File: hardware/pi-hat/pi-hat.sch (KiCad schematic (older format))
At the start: 100 parts, among them J1 PWR_IN, J10 6-8, J11 LED0, J12 LED1, J13 KLPX-0848A-2-B, J14 KLPX-0848A-2-R, J2 A-F, J3 40HAT, J4 G-M, J5 N-Q, J6 PANEL_PWR, J7 PANEL_CTL, J8 2-5, J9 WP, Q1 DMG2305UX, Q2 DMMT5401, Q3 DMN6075S, Q4 DMP4065S, Q5 DMN6075S, U1 CAT24C32, U10 L78L33_SOT89, U11 L78L33_SOT89, U12 PCM5122PW, U13 TSR_2-2450, U14 TSR_2-2450, U15 TSR_2-2450, U2 CM1293A, U3 CM1293A, U4 CM1293A, U5 CM1293A, U6 CM1293A, U7 CM1293A, U8 MCP23S17_SO, U9 MCP23S17_SO

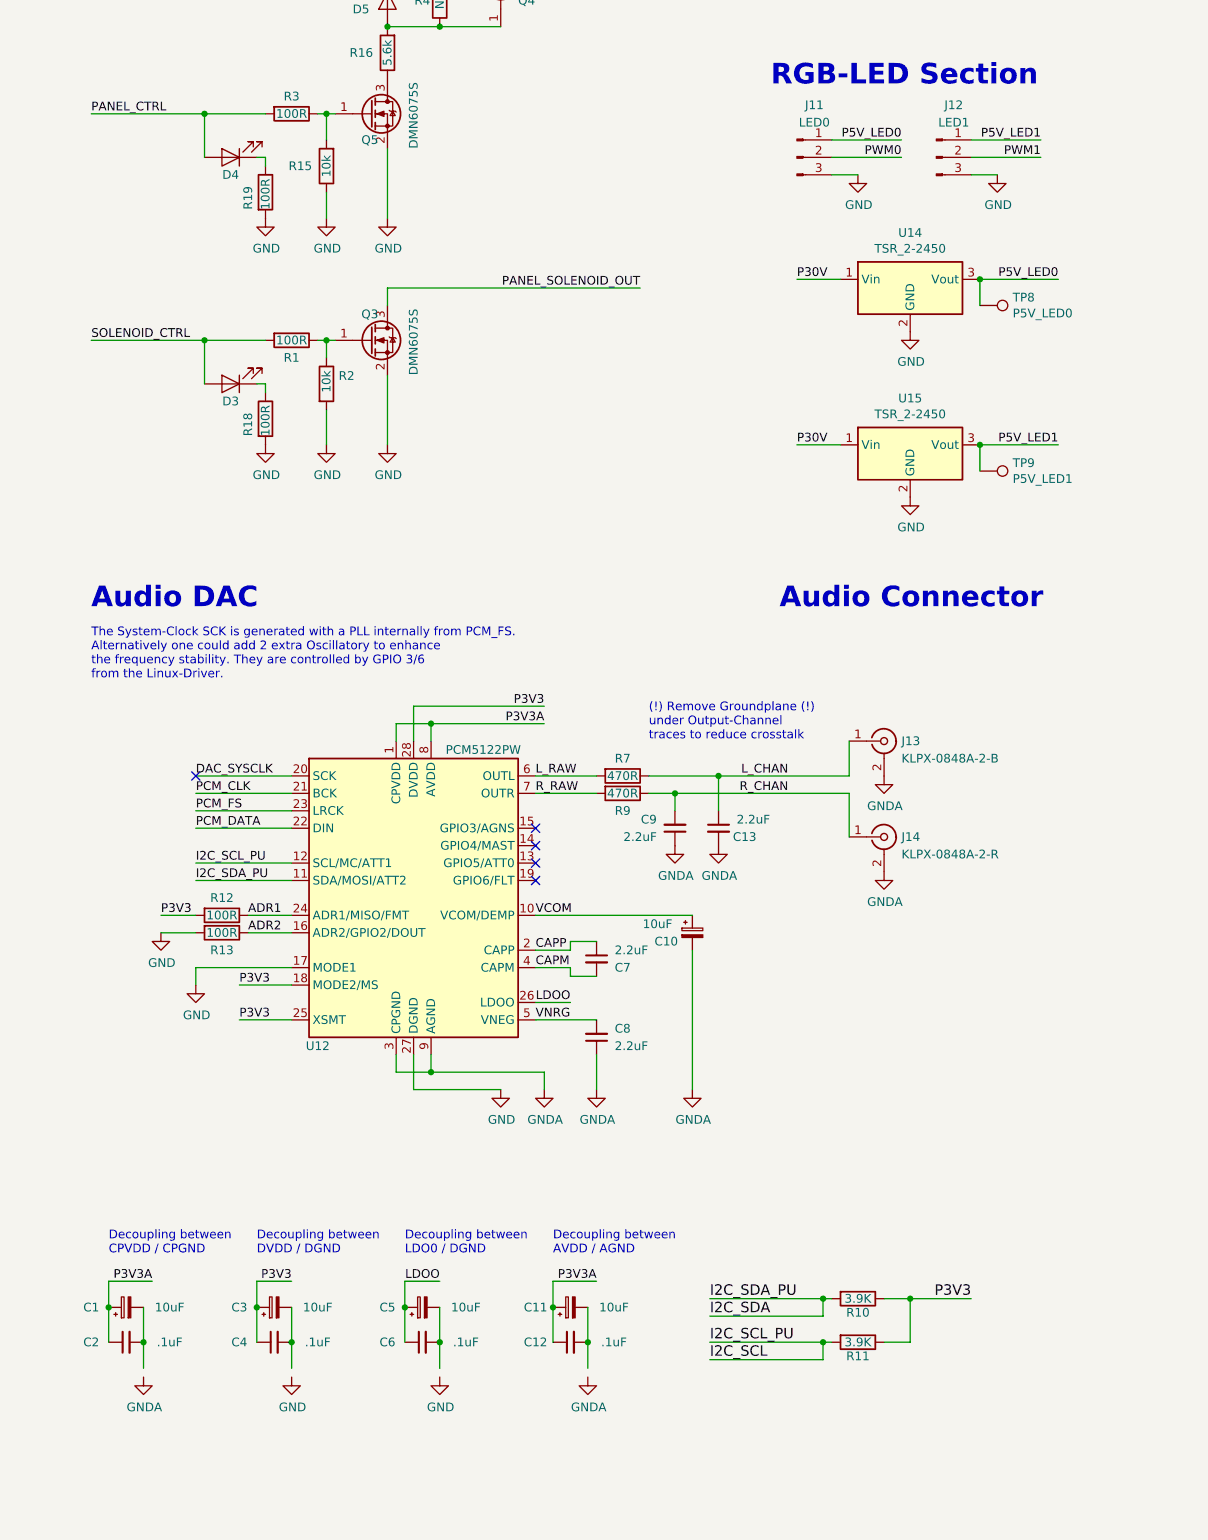
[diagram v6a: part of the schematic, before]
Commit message: fix broken gnd, only install a single 5V 2A DC/DC for the LEDs
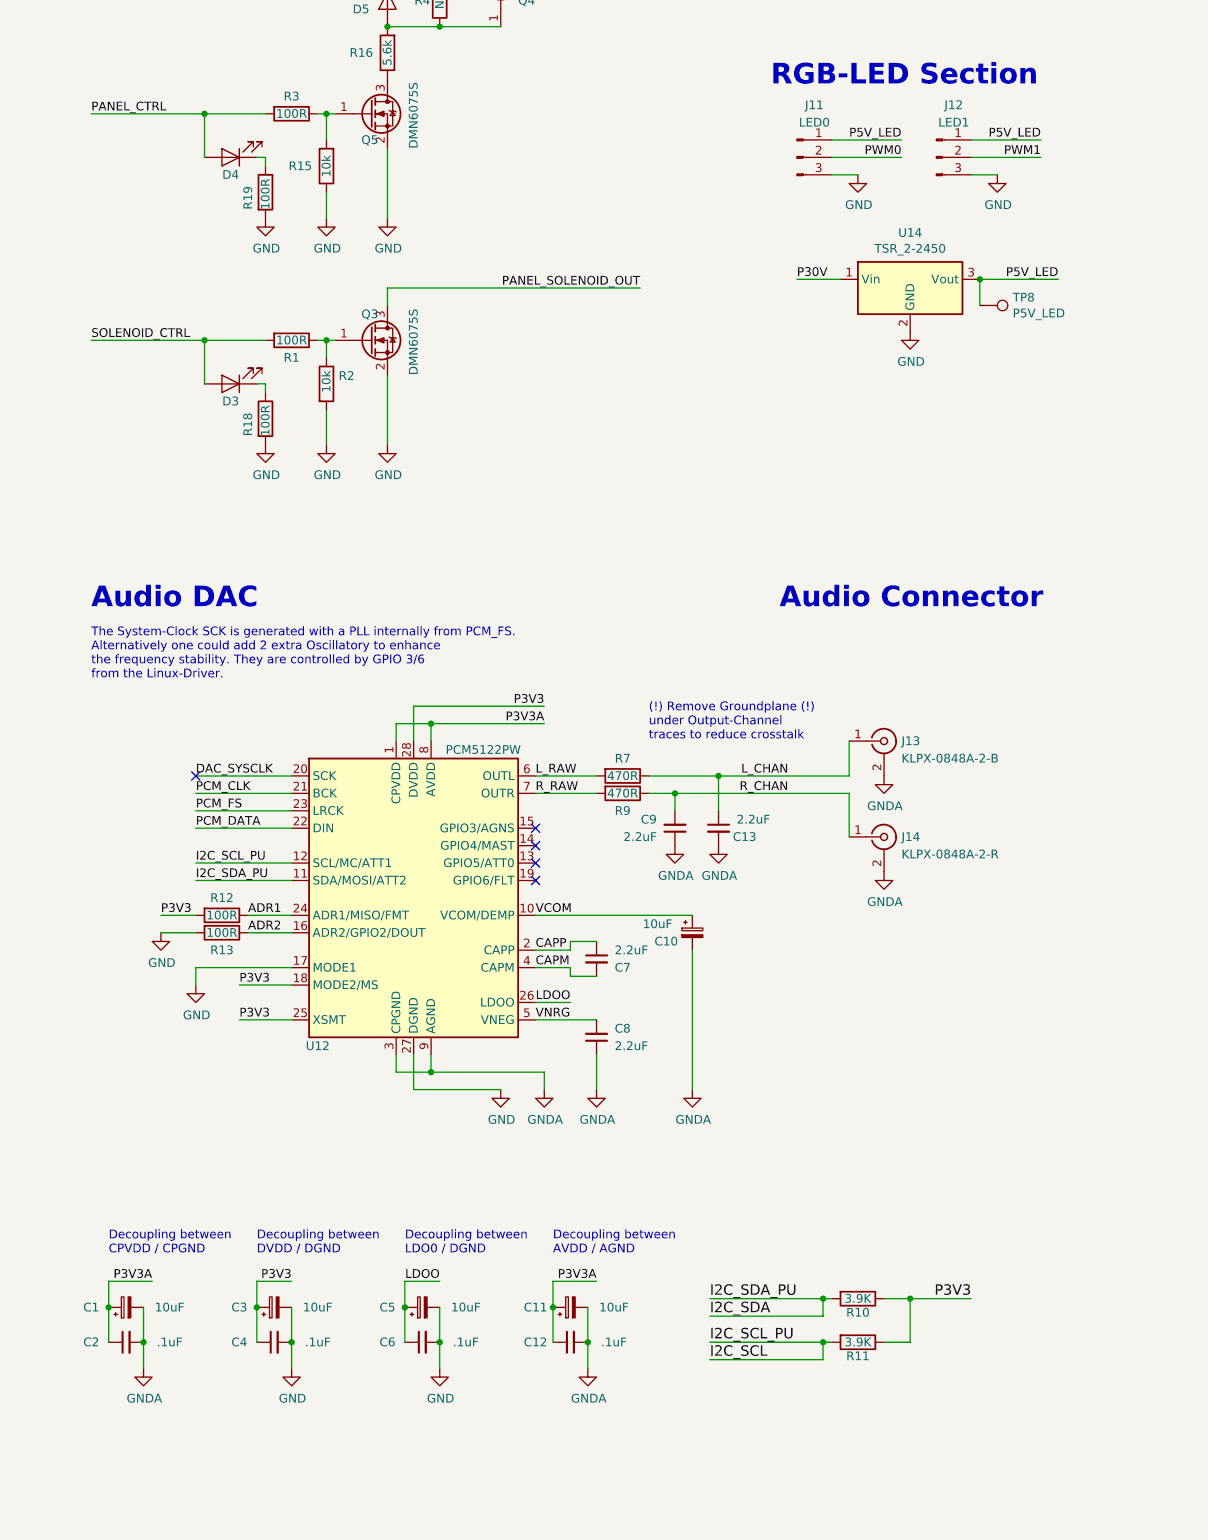
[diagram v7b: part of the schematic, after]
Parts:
- removed TP9: P5V_LED1, TestPoint:TestPoint_Pad_D1.5mm, symbol Connector:TestPoint
- removed U15: TSR_2-2450, Converter_DCDC:Converter_DCDC_TRACO_TSR-1_THT, symbol Regulator_Switching:TSR_1-2450
- TP8: value P5V_LED0 -> P5V_LED
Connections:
- net P5V_LED1 is gone; now on net P5V_LED: J12.1 (Pin_1)
- net GND: now also C3.2, C4.2, C5.2, C6.2
- net GNDA: now also C1.2, C11.2, C12.2, C2.2
- net P5V_LED0 renamed P5V_LED
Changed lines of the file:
@@
 L power:GND #PWR0109
 U 1 1 60FE9052
-P 6300 13200
-F 0 "#PWR0109" H 6300 12950 50  0001 C CNN
-F 1 "GND" H 6305 13027 50  0000 C CNN
-F 2 "" H 6300 13200 50  0001 C CNN
-F 3 "" H 6300 13200 50  0001 C CNN
-	1    6300 13200
+P 6300 13150
+F 0 "#PWR0109" H 6300 12900 50  0001 C CNN
+F 1 "GND" H 6305 12977 50  0000 C CNN
+F 2 "" H 6300 13150 50  0001 C CNN
+F 3 "" H 6300 13150 50  0001 C CNN
+	1    6300 13150
 	1    0    0    -1
 $EndComp
@@
 L power:GND #PWR0110
 U 1 1 610983C0
-P 7150 13200
-F 0 "#PWR0110" H 7150 12950 50  0001 C CNN
-F 1 "GND" H 7155 13027 50  0000 C CNN
-F 2 "" H 7150 13200 50  0001 C CNN
-F 3 "" H 7150 13200 50  0001 C CNN
-	1    7150 13200
+P 7150 13150
+F 0 "#PWR0110" H 7150 12900 50  0001 C CNN
+F 1 "GND" H 7155 12977 50  0000 C CNN
+F 2 "" H 7150 13150 50  0001 C CNN
+F 3 "" H 7150 13150 50  0001 C CNN
+	1    7150 13150
 	1    0    0    -1
 $EndComp
@@
 L power:GNDA #PWR0111
 U 1 1 6124BBFC
-P 5450 13200
-F 0 "#PWR0111" H 5450 12950 50  0001 C CNN
-F 1 "GNDA" H 5455 13027 50  0000 C CNN
-F 2 "" H 5450 13200 50  0001 C CNN
-F 3 "" H 5450 13200 50  0001 C CNN
-	1    5450 13200
+P 5450 13150
+F 0 "#PWR0111" H 5450 12900 50  0001 C CNN
+F 1 "GNDA" H 5455 12977 50  0000 C CNN
+F 2 "" H 5450 13150 50  0001 C CNN
+F 3 "" H 5450 13150 50  0001 C CNN
+	1    5450 13150
 	1    0    0    -1
 $EndComp
@@
 L power:GNDA #PWR0115
 U 1 1 617E7560
-P 8000 13200
-F 0 "#PWR0115" H 8000 12950 50  0001 C CNN
-F 1 "GNDA" H 8005 13027 50  0000 C CNN
-F 2 "" H 8000 13200 50  0001 C CNN
-F 3 "" H 8000 13200 50  0001 C CNN
-	1    8000 13200
+P 8000 13150
+F 0 "#PWR0115" H 8000 12900 50  0001 C CNN
+F 1 "GNDA" H 8005 12977 50  0000 C CNN
+F 2 "" H 8000 13150 50  0001 C CNN
+F 3 "" H 8000 13150 50  0001 C CNN
+	1    8000 13150
 	1    0    0    -1
 $EndComp
@@
 	7150 5150 7300 5150
 Text Label 10700 6900 2    50   ~ 0
-P5V_LED0
+P5V_LED
 $Comp
 L Connector:TestPoint TP8
@@
 P 10250 7050
 F 0 "TP8" V 10204 7238 50  0000 L CNN
-F 1 "P5V_LED0" V 10295 7238 50  0000 L CNN
+F 1 "P5V_LED" V 10295 7238 50  0000 L CNN
 F 2 "TestPoint:TestPoint_Pad_D1.5mm" H 10450 7050 50  0001 C CNN
 F 3 "~" H 10450 7050 50  0001 C CNN
@@
 	10200 6100 10600 6100
 Text Label 9800 6100 2    50   ~ 0
-P5V_LED0
+P5V_LED
 Text Label 10600 6100 2    50   ~ 0
-P5V_LED1
-Text Label 10700 7850 2    50   ~ 0
-P5V_LED1
-$Comp
-L Connector:TestPoint TP9
-U 1 1 5E6661C1
-P 10250 8000
-F 0 "TP9" V 10204 8188 50  0000 L CNN
-F 1 "P5V_LED1" V 10295 8188 50  0000 L CNN
-F 2 "TestPoint:TestPoint_Pad_D1.5mm" H 10450 8000 50  0001 C CNN
-F 3 "~" H 10450 8000 50  0001 C CNN
-	1    10250 8000
-	0    1    1    0
-$EndComp
-$Comp
-L Regulator_Switching:TSR_1-2450 U15
-U 1 1 5E6661C7
-P 9850 7950
-F 0 "U15" H 9850 8317 50  0000 C CNN
-F 1 "TSR_2-2450" H 9850 8226 50  0000 C CNN
-F 2 "Converter_DCDC:Converter_DCDC_TRACO_TSR-1_THT" H 9850 7800 50  0001 L CIN
-F 3 "http://www.tracopower.com/products/tsr1.pdf" H 9850 7950 50  0001 C CNN
-	1    9850 7950
-	1    0    0    -1
-$EndComp
-Wire Wire Line
-	10250 7850 10700 7850
-Wire Wire Line
-	9450 7850 9200 7850
-Text Label 9200 7850 0    50   ~ 0
-P30V
-$Comp
-L power:GND #PWR0128
-U 1 1 5E6661D0
-P 9850 8150
-F 0 "#PWR0128" H 9850 7900 50  0001 C CNN
-F 1 "GND" H 9855 7977 50  0000 C CNN
-F 2 "" H 9850 8150 50  0001 C CNN
-F 3 "" H 9850 8150 50  0001 C CNN
-	1    9850 8150
-	1    0    0    -1
-$EndComp
-Wire Wire Line
-	10250 7850 10250 8000
-Connection ~ 10250 7850
+P5V_LED
 Wire Wire Line
 	6300 9750 5750 9750

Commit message: insert correct WUERTH footprint
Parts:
- J1: footprint TerminalBlock:TerminalBlock_bornier-2_P5.08mm -> project_footprints:WUERTH-2-5mm
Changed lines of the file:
@@
 F 0 "J1" H 9550 2100 50  0000 C CNN
 F 1 "PWR_IN" H 9550 2200 50  0000 C CNN
-F 2 "TerminalBlock:TerminalBlock_bornier-2_P5.08mm" H 9450 2450 50  0001 C CNN
+F 2 "project_footprints:WUERTH-2-5mm" H 9450 2450 50  0001 C CNN
 F 3 "~" H 9450 2450 50  0001 C CNN
 	1    9450 2450
